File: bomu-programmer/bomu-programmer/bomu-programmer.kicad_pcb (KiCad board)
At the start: 2 copper layers, 13.4 x 10.2 mm, 2 parts, among them J1 Conn_ARM_JTAG_SWD_10, P1 1mm_pitch_2x4

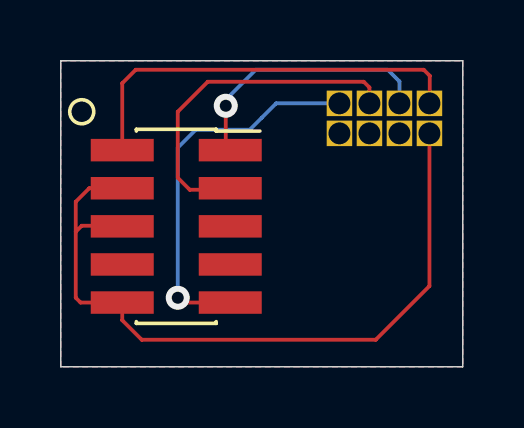
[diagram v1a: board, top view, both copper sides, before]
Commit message: Updating for KiCAD 7. Updated bomu-programmer board. Gerbers for bomu-programmer generated.
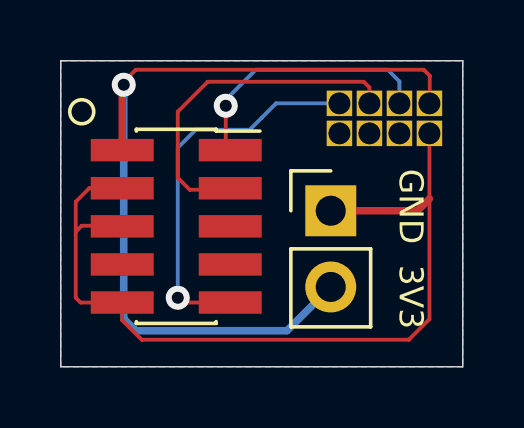
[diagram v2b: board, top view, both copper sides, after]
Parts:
- added J2: Conn_01x02, Connector_PinHeader_2.54mm:PinHeader_1x02_P2.54mm_Vertical, F.Cu at (201.9, 56.3)
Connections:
- net RESET renamed Net-(J1-~{RESET})
- net SWDCLK renamed Net-(J1-SWDCLK/TCK)
- net SWDIO renamed Net-(J1-SWDIO/TMS)
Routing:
- net +3V3: track 13.7 -> 29.2 mm, vias 0 -> 1
- net GND: track 25.1 -> 29.2 mm
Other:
- board text added: "3V3"
- board text added: "GND"
